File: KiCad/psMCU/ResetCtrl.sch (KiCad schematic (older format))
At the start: 14 parts

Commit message: Pulled in from clock test, root layout first draft
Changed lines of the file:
@@
 $Descr A4 11693 8268
 encoding utf-8
-Sheet 111 193
+Sheet 113 209
 Title "psMCU"
 Date ""
@@
 AR Path="/5F1CE57C/5FD43FAC" Ref="#PWR?"  Part="1"
 AR Path="/608BF85D/5FD43FAC" Ref="#PWR?"  Part="1"
-AR Path="/5FD3CD07/5FD43FAC" Ref="#PWR?"  Part="1"
-F 0 "#PWR?" H 8850 3100 50  0001 C CNN
+AR Path="/5FD3CD07/5FD43FAC" Ref="#PWR01660"  Part="1"
+F 0 "#PWR01660" H 8850 3100 50  0001 C CNN
 F 1 "GND" V 8855 3222 50  0000 R CNN
 F 2 "" H 8850 3350 50  0001 C CNN
@@
 AR Path="/5F1CE57C/5FD43FB4" Ref="#PWR?"  Part="1"
 AR Path="/608BF85D/5FD43FB4" Ref="#PWR?"  Part="1"
-AR Path="/5FD3CD07/5FD43FB4" Ref="#PWR?"  Part="1"
-F 0 "#PWR?" H 8550 3500 50  0001 C CNN
+AR Path="/5FD3CD07/5FD43FB4" Ref="#PWR01661"  Part="1"
+F 0 "#PWR01661" H 8550 3500 50  0001 C CNN
 F 1 "GND" H 8555 3577 50  0000 C CNN
 F 2 "" H 8550 3750 50  0001 C CNN
@@
 AR Path="/5F1CE57C/5FD43FC2" Ref="#PWR?"  Part="1"
 AR Path="/608BF85D/5FD43FC2" Ref="#PWR?"  Part="1"
-AR Path="/5FD3CD07/5FD43FC2" Ref="#PWR?"  Part="1"
-F 0 "#PWR?" H 8550 3150 50  0001 C CNN
+AR Path="/5FD3CD07/5FD43FC2" Ref="#PWR01662"  Part="1"
+F 0 "#PWR01662" H 8550 3150 50  0001 C CNN
 F 1 "+5V" H 8450 3400 50  0000 C CNN
 F 2 "" H 8550 3300 50  0001 C CNN
@@
 	8800 3550 9350 3550
 Wire Wire Line
-	9350 4000 7800 4000
+	9350 4000 8250 4000
 Wire Wire Line
 	7800 4000 7800 3550
@@
 AR Path="/5F1CE57C/5FF7364D" Ref="#PWR?"  Part="1"
 AR Path="/5F396002/5FF7364D" Ref="#PWR?"  Part="1"
-AR Path="/5FD3CD07/5FF7364D" Ref="#PWR?"  Part="1"
-F 0 "#PWR?" H 5850 3150 50  0001 C CNN
+AR Path="/5FD3CD07/5FF7364D" Ref="#PWR01663"  Part="1"
+F 0 "#PWR01663" H 5850 3150 50  0001 C CNN
 F 1 "GND" H 5855 3227 50  0000 C CNN
 F 2 "" H 5850 3400 50  0001 C CNN
@@
 AR Path="/5F1CE57C/5FF73655" Ref="#PWR?"  Part="1"
 AR Path="/5F396002/5FF73655" Ref="#PWR?"  Part="1"
-AR Path="/5FD3CD07/5FF73655" Ref="#PWR?"  Part="1"
-F 0 "#PWR?" H 5850 2800 50  0001 C CNN
+AR Path="/5FD3CD07/5FF73655" Ref="#PWR01664"  Part="1"
+F 0 "#PWR01664" H 5850 2800 50  0001 C CNN
 F 1 "+5V" H 5865 3123 50  0000 C CNN
 F 2 "" H 5850 2950 50  0001 C CNN
@@
 AR Path="/5F1CE57C/5FF73664" Ref="#PWR?"  Part="1"
 AR Path="/5F396002/5FF73664" Ref="#PWR?"  Part="1"
-AR Path="/5FD3CD07/5FF73664" Ref="#PWR?"  Part="1"
-F 0 "#PWR?" H 6150 2750 50  0001 C CNN
+AR Path="/5FD3CD07/5FF73664" Ref="#PWR01665"  Part="1"
+F 0 "#PWR01665" H 6150 2750 50  0001 C CNN
 F 1 "GND" V 6155 2872 50  0000 R CNN
 F 2 "" H 6150 3000 50  0001 C CNN
@@
 AR Path="/5F1CE57C/5FFDD1F3" Ref="#PWR?"  Part="1"
 AR Path="/5F396002/5FFDD1F3" Ref="#PWR?"  Part="1"
-AR Path="/5FD3CD07/5FFDD1F3" Ref="#PWR?"  Part="1"
-F 0 "#PWR?" H 3450 2700 50  0001 C CNN
+AR Path="/5FD3CD07/5FFDD1F3" Ref="#PWR01666"  Part="1"
+F 0 "#PWR01666" H 3450 2700 50  0001 C CNN
 F 1 "GND" V 3455 2822 50  0000 R CNN
 F 2 "" H 3450 2950 50  0001 C CNN
@@
 AR Path="/5F1CE57C/5FFDD202" Ref="#PWR?"  Part="1"
 AR Path="/5F396002/5FFDD202" Ref="#PWR?"  Part="1"
-AR Path="/5FD3CD07/5FFDD202" Ref="#PWR?"  Part="1"
-F 0 "#PWR?" H 3150 2750 50  0001 C CNN
+AR Path="/5FD3CD07/5FFDD202" Ref="#PWR01667"  Part="1"
+F 0 "#PWR01667" H 3150 2750 50  0001 C CNN
 F 1 "+5V" H 3165 3073 50  0000 C CNN
 F 2 "" H 3150 2900 50  0001 C CNN
@@
 AR Path="/5F1CE57C/5FFDD209" Ref="#PWR?"  Part="1"
 AR Path="/5F396002/5FFDD209" Ref="#PWR?"  Part="1"
-AR Path="/5FD3CD07/5FFDD209" Ref="#PWR?"  Part="1"
-F 0 "#PWR?" H 3150 3050 50  0001 C CNN
+AR Path="/5FD3CD07/5FFDD209" Ref="#PWR01668"  Part="1"
+F 0 "#PWR01668" H 3150 3050 50  0001 C CNN
 F 1 "GND" H 3250 3150 50  0000 R CNN
 F 2 "" H 3150 3300 50  0001 C CNN
@@
 AR Path="/5F1CE57C/5FFDEBBC" Ref="#PWR?"  Part="1"
 AR Path="/5F396002/5FFDEBBC" Ref="#PWR?"  Part="1"
-AR Path="/5FD3CD07/5FFDEBBC" Ref="#PWR?"  Part="1"
-F 0 "#PWR?" H 2400 3250 50  0001 C CNN
+AR Path="/5FD3CD07/5FFDEBBC" Ref="#PWR01669"  Part="1"
+F 0 "#PWR01669" H 2400 3250 50  0001 C CNN
 F 1 "GND" H 2500 3350 50  0000 R CNN
 F 2 "" H 2400 3500 50  0001 C CNN
@@
 AR Path="/5F1CE57C/5FFE9777" Ref="#PWR?"  Part="1"
 AR Path="/5F396002/5FFE9777" Ref="#PWR?"  Part="1"
-AR Path="/5FD3CD07/5FFE9777" Ref="#PWR?"  Part="1"
-F 0 "#PWR?" H 2400 2350 50  0001 C CNN
+AR Path="/5FD3CD07/5FFE9777" Ref="#PWR01670"  Part="1"
+F 0 "#PWR01670" H 2400 2350 50  0001 C CNN
 F 1 "+5V" H 2415 2673 50  0000 C CNN
 F 2 "" H 2400 2500 50  0001 C CNN
@@
 AR Path="/5F1CE57C/6000A97B" Ref="#PWR?"  Part="1"
 AR Path="/608BF85D/6000A97B" Ref="#PWR?"  Part="1"
-AR Path="/5FD3CD07/6000A97B" Ref="#PWR?"  Part="1"
-F 0 "#PWR?" H 4300 2700 50  0001 C CNN
+AR Path="/5FD3CD07/6000A97B" Ref="#PWR01671"  Part="1"
+F 0 "#PWR01671" H 4300 2700 50  0001 C CNN
 F 1 "GND" V 4305 2822 50  0000 R CNN
 F 2 "" H 4300 2950 50  0001 C CNN
@@
 AR Path="/5F1CE57C/6000A983" Ref="#PWR?"  Part="1"
 AR Path="/608BF85D/6000A983" Ref="#PWR?"  Part="1"
-AR Path="/5FD3CD07/6000A983" Ref="#PWR?"  Part="1"
-F 0 "#PWR?" H 4000 3100 50  0001 C CNN
+AR Path="/5FD3CD07/6000A983" Ref="#PWR01672"  Part="1"
+F 0 "#PWR01672" H 4000 3100 50  0001 C CNN
 F 1 "GND" H 4005 3177 50  0000 C CNN
 F 2 "" H 4000 3350 50  0001 C CNN
@@
 AR Path="/5F1CE57C/6000A991" Ref="#PWR?"  Part="1"
 AR Path="/608BF85D/6000A991" Ref="#PWR?"  Part="1"
-AR Path="/5FD3CD07/6000A991" Ref="#PWR?"  Part="1"
-F 0 "#PWR?" H 4000 2750 50  0001 C CNN
+AR Path="/5FD3CD07/6000A991" Ref="#PWR01673"  Part="1"
+F 0 "#PWR01673" H 4000 2750 50  0001 C CNN
 F 1 "+5V" H 3900 3000 50  0000 C CNN
 F 2 "" H 4000 2900 50  0001 C CNN
@@
 AR Path="/5F1CE57C/61C134A2" Ref="#PWR?"  Part="1"
 AR Path="/5F396002/61C134A2" Ref="#PWR?"  Part="1"
-AR Path="/5FD3CD07/61C134A2" Ref="#PWR?"  Part="1"
-F 0 "#PWR?" H 7100 3200 50  0001 C CNN
+AR Path="/5FD3CD07/61C134A2" Ref="#PWR01674"  Part="1"
+F 0 "#PWR01674" H 7100 3200 50  0001 C CNN
 F 1 "GND" H 7105 3277 50  0000 C CNN
 F 2 "" H 7100 3450 50  0001 C CNN
@@
 AR Path="/5F1CE57C/61C134AA" Ref="#PWR?"  Part="1"
 AR Path="/5F396002/61C134AA" Ref="#PWR?"  Part="1"
-AR Path="/5FD3CD07/61C134AA" Ref="#PWR?"  Part="1"
-F 0 "#PWR?" H 7100 2850 50  0001 C CNN
+AR Path="/5FD3CD07/61C134AA" Ref="#PWR01675"  Part="1"
+F 0 "#PWR01675" H 7100 2850 50  0001 C CNN
 F 1 "+5V" H 7115 3173 50  0000 C CNN
 F 2 "" H 7100 3000 50  0001 C CNN
@@
 AR Path="/5F1CE57C/61C134B9" Ref="#PWR?"  Part="1"
 AR Path="/5F396002/61C134B9" Ref="#PWR?"  Part="1"
-AR Path="/5FD3CD07/61C134B9" Ref="#PWR?"  Part="1"
-F 0 "#PWR?" H 7400 2800 50  0001 C CNN
+AR Path="/5FD3CD07/61C134B9" Ref="#PWR01676"  Part="1"
+F 0 "#PWR01676" H 7400 2800 50  0001 C CNN
 F 1 "GND" V 7405 2922 50  0000 R CNN
 F 2 "" H 7400 3050 50  0001 C CNN
@@
 Wire Wire Line
 	5300 3150 5550 3150
+$Sheet
+S 8650 4350 700  200
+U 602A39E5
+F0 "LED: Reset" 50
+F1 "1BitLED.sch" 50
+F2 "VAL" I L 8650 4450 50
+$EndSheet
+Wire Wire Line
+	8650 4450 8250 4450
+Wire Wire Line
+	8250 4450 8250 4000
+Connection ~ 8250 4000
+Wire Wire Line
+	8250 4000 7800 4000
 $EndSCHEMATC

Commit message: Added some footprints, small optimisations
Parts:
- U? (x3): footprint (none) -> Package_TO_SOT_SMD:SOT-353_SC-70-5
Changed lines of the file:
@@
 $Descr A4 11693 8268
 encoding utf-8
-Sheet 113 202
+Sheet 147 202
 Title "psMCU"
 Date ""
@@
 F 0 "U?" H 6000 3100 50  0000 C CNN
 F 1 "74LVC1G32" H 6150 3000 50  0000 C CNN
-F 2 "" H 5850 3200 50  0001 C CNN
+F 2 "Package_TO_SOT_SMD:SOT-353_SC-70-5" H 5850 3200 50  0001 C CNN
 F 3 "http://www.ti.com/lit/sg/scyt129e/scyt129e.pdf" H 5850 3200 50  0001 C CNN
 	1    5850 3200
@@
 F 0 "U?" H 3300 3100 50  0000 C CNN
 F 1 "74LVC1G17" H 3450 3000 50  0000 C CNN
-F 2 "" H 3150 3150 50  0001 C CNN
+F 2 "Package_TO_SOT_SMD:SOT-353_SC-70-5" H 3150 3150 50  0001 C CNN
 F 3 "http://www.ti.com/lit/sg/scyt129e/scyt129e.pdf" H 3150 3150 50  0001 C CNN
 	1    3150 3150
@@
 F 0 "U?" H 7250 3150 50  0000 C CNN
 F 1 "74LVC1G32" H 7400 3050 50  0000 C CNN
-F 2 "" H 7100 3250 50  0001 C CNN
+F 2 "Package_TO_SOT_SMD:SOT-353_SC-70-5" H 7100 3250 50  0001 C CNN
 F 3 "http://www.ti.com/lit/sg/scyt129e/scyt129e.pdf" H 7100 3250 50  0001 C CNN
 	1    7100 3250

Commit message: Started some documentation work.
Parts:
- R?: value 56k -> 1M
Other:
- note added: "Automatic Reset on Power-on"
- note added: "Combine Reset Sources"
- note removed: "Automatic Reset-on-Power"
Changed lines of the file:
@@
 Comment1 ""
 Comment2 ""
-Comment3 ""
-Comment4 ""
+Comment3 "generate the RESET and ~RESET~ signals used globally."
+Comment4 "Generates reset during power-on and combines the different reset sources to"
 $EndDescr
 Text Label 9250 3550 2    50   ~ 0
@@
 P 2400 2950
 F 0 "R?" H 2459 2996 50  0000 L CNN
-F 1 "56k" H 2459 2905 50  0000 L CNN
+F 1 "1M" H 2459 2905 50  0000 L CNN
 F 2 "Resistor_SMD:R_0603_1608Metric" H 2400 2950 50  0001 C CNN
 F 3 "~" H 2400 2950 50  0001 C CNN
@@
 Wire Wire Line
 	7800 3250 7800 3550
-Text Notes 3000 2450 0    50   ~ 0
-Automatic Reset-on-Power
-Text HLabel 7000 2450 2    50   Output ~ 0
+Text Notes 1950 1850 0    100  ~ 0
+Automatic Reset on Power-on
+Text HLabel 5400 2450 2    50   Output ~ 0
 POWER_ON_RESET
 Wire Wire Line
 	5300 2450 5300 3150
 Wire Wire Line
-	5300 2450 7000 2450
+	5300 2450 5400 2450
 Connection ~ 5300 3150
 Wire Wire Line
@@
 Wire Wire Line
 	8250 4000 7800 4000
+Text Notes 5750 1850 0    100  ~ 0
+Combine Reset Sources
 $EndSCHEMATC

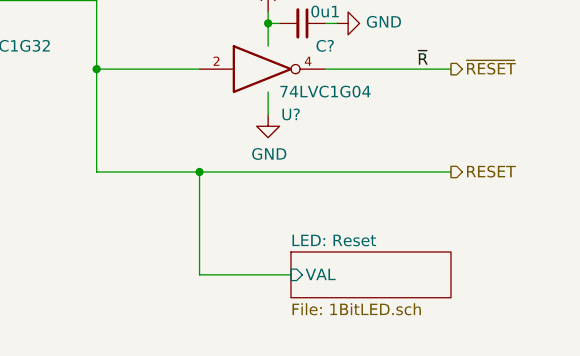
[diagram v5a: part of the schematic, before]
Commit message: Removed Single LED sheets
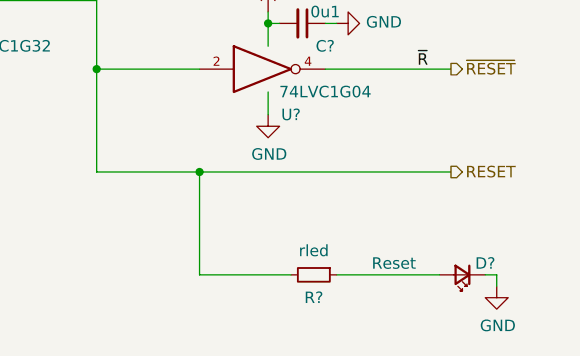
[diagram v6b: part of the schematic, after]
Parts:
- added D?: Reset, Diode_SMD:D_0603_1608Metric, symbol Device:LED_Small
- added R?: rled, Resistor_SMD:R_0603_1608Metric, symbol Device:R_Small
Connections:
- net GND: now also D?.1 (K)
- net RESET: now also R?.2
- new net: D?.2 (A), R?.1

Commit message: First Schematic Draft done.
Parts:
- removed C? (x2): 0u1, Capacitor_SMD:C_0603_1608Metric, symbol Device:C_Small
- removed U? (x2): 74LVC1G32, Package_TO_SOT_SMD:SOT-353_SC-70-5, symbol 74xGxx:74LVC1G32
- added C285: 0u1, NoRef_Footprints:C_0603_1608Metric_NoRef, symbol Device:C_Small
- added U279: 74LVC1G332, symbol 74xGxx:74LVC1G332
- C282, C283, C284, C286: renamed from C?; footprint Capacitor_SMD:C_0603_1608Metric -> NoRef_Footprints:C_0603_1608Metric_NoRef
- D362: renamed from D?; footprint Diode_SMD:D_0603_1608Metric -> NoRef_Footprints:D_0603_1608Metric_NoRef
- R367: renamed from R?; footprint Resistor_SMD:R_0603_1608Metric -> NoRef_Footprints:R_0603_1608Metric
- gave numbers to parts that had none: 6
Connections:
- net +5V: now also C285.2, U279.5 (VCC)
- net GND: now also C285.1, U279.2 (GND)
- net POWER_ON_RESET: now also U279.6
- net PROG_DO_RESET: now also U279.3
- net RESET: now also U279.4
- net UI_DO_RESET: now also U279.1
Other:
- note added: "Generate different Reset signals"
- note removed: "Combine Reset Sources"
- moved on the sheet: C286, D362, R367, U280

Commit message: Small improvements.
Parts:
- renumbered C282 to C280, C283 to C281, C284 to C282, C285 to C283, C286 to C284, U277 to U275, U278 to U276, U279 to U277, U280 to U278
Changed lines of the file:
@@
 AR Path="/5F1CE57C/5FD43FAC" Ref="#PWR?"  Part="1"
 AR Path="/608BF85D/5FD43FAC" Ref="#PWR?"  Part="1"
-AR Path="/5FD3CD07/5FD43FAC" Ref="#PWR01237"  Part="1"
-F 0 "#PWR01237" H 7750 3100 50  0001 C CNN
+AR Path="/5FD3CD07/5FD43FAC" Ref="#PWR01222"  Part="1"
+F 0 "#PWR01222" H 7750 3100 50  0001 C CNN
 F 1 "GND" V 7755 3222 50  0000 R CNN
 F 2 "" H 7750 3350 50  0001 C CNN
@@
 AR Path="/5F1CE57C/5FD43FB4" Ref="#PWR?"  Part="1"
 AR Path="/608BF85D/5FD43FB4" Ref="#PWR?"  Part="1"
-AR Path="/5FD3CD07/5FD43FB4" Ref="#PWR01236"  Part="1"
-F 0 "#PWR01236" H 7450 3500 50  0001 C CNN
+AR Path="/5FD3CD07/5FD43FB4" Ref="#PWR01221"  Part="1"
+F 0 "#PWR01221" H 7450 3500 50  0001 C CNN
 F 1 "GND" H 7455 3577 50  0000 C CNN
 F 2 "" H 7450 3750 50  0001 C CNN
@@
 AR Path="/5F1CE57C/5FD43FBC" Ref="C?"  Part="1"
 AR Path="/608BF85D/5FD43FBC" Ref="C?"  Part="1"
-AR Path="/5FD3CD07/5FD43FBC" Ref="C286"  Part="1"
-F 0 "C286" V 7700 3450 50  0000 C CNN
+AR Path="/5FD3CD07/5FD43FBC" Ref="C284"  Part="1"
+F 0 "C284" V 7700 3450 50  0000 C CNN
 F 1 "0u1" V 7550 3450 50  0000 C CNN
 F 2 "NoRef_Footprints:C_0603_1608Metric_NoRef" H 7600 3350 50  0001 C CNN
@@
 AR Path="/5F1CE57C/5FD43FC2" Ref="#PWR?"  Part="1"
 AR Path="/608BF85D/5FD43FC2" Ref="#PWR?"  Part="1"
-AR Path="/5FD3CD07/5FD43FC2" Ref="#PWR01235"  Part="1"
-F 0 "#PWR01235" H 7450 3150 50  0001 C CNN
+AR Path="/5FD3CD07/5FD43FC2" Ref="#PWR01220"  Part="1"
+F 0 "#PWR01220" H 7450 3150 50  0001 C CNN
 F 1 "+5V" H 7350 3400 50  0000 C CNN
 F 2 "" H 7450 3300 50  0001 C CNN
@@
 AR Path="/5F1CE57C/5FD43FCA" Ref="U?"  Part="1"
 AR Path="/608BF85D/5FD43FCA" Ref="U?"  Part="1"
-AR Path="/5FD3CD07/5FD43FCA" Ref="U280"  Part="1"
-F 0 "U280" H 7550 3350 50  0000 C CNN
+AR Path="/5FD3CD07/5FD43FCA" Ref="U278"  Part="1"
+F 0 "U278" H 7550 3350 50  0000 C CNN
 F 1 "74LVC1G04" H 7700 3450 50  0000 C CNN
 F 2 "Package_TO_SOT_SMD:SOT-353_SC-70-5" H 7450 3550 50  0001 C CNN
@@
 UI_DO_RESET
 $Comp
-L 74xGxx:74LVC1G17 U277
+L 74xGxx:74LVC1G17 U275
 U 1 1 5FFDD1EC
 P 3150 3150
-F 0 "U277" H 3300 3100 50  0000 C CNN
+F 0 "U275" H 3300 3100 50  0000 C CNN
 F 1 "74LVC1G17" H 3450 3000 50  0000 C CNN
 F 2 "Package_TO_SOT_SMD:SOT-353_SC-70-5" H 3150 3150 50  0001 C CNN
@@
 AR Path="/5F1CE57C/5FFDD1F3" Ref="#PWR?"  Part="1"
 AR Path="/5F396002/5FFDD1F3" Ref="#PWR?"  Part="1"
-AR Path="/5FD3CD07/5FFDD1F3" Ref="#PWR01228"  Part="1"
-F 0 "#PWR01228" H 3450 2700 50  0001 C CNN
+AR Path="/5FD3CD07/5FFDD1F3" Ref="#PWR01213"  Part="1"
+F 0 "#PWR01213" H 3450 2700 50  0001 C CNN
 F 1 "GND" V 3455 2822 50  0000 R CNN
 F 2 "" H 3450 2950 50  0001 C CNN
@@
 AR Path="/5F1CE57C/5FFDD1FC" Ref="C?"  Part="1"
 AR Path="/5F396002/5FFDD1FC" Ref="C?"  Part="1"
-AR Path="/5FD3CD07/5FFDD1FC" Ref="C283"  Part="1"
-F 0 "C283" V 3400 3050 50  0000 C CNN
+AR Path="/5FD3CD07/5FFDD1FC" Ref="C281"  Part="1"
+F 0 "C281" V 3400 3050 50  0000 C CNN
 F 1 "0u1" V 3250 3050 50  0000 C CNN
 F 2 "NoRef_Footprints:C_0603_1608Metric_NoRef" H 3300 2950 50  0001 C CNN
@@
 AR Path="/5F1CE57C/5FFDD202" Ref="#PWR?"  Part="1"
 AR Path="/5F396002/5FFDD202" Ref="#PWR?"  Part="1"
-AR Path="/5FD3CD07/5FFDD202" Ref="#PWR01226"  Part="1"
-F 0 "#PWR01226" H 3150 2750 50  0001 C CNN
+AR Path="/5FD3CD07/5FFDD202" Ref="#PWR01211"  Part="1"
+F 0 "#PWR01211" H 3150 2750 50  0001 C CNN
 F 1 "+5V" H 3165 3073 50  0000 C CNN
 F 2 "" H 3150 2900 50  0001 C CNN
@@
 AR Path="/5F1CE57C/5FFDD209" Ref="#PWR?"  Part="1"
 AR Path="/5F396002/5FFDD209" Ref="#PWR?"  Part="1"
-AR Path="/5FD3CD07/5FFDD209" Ref="#PWR01227"  Part="1"
-F 0 "#PWR01227" H 3150 3050 50  0001 C CNN
+AR Path="/5FD3CD07/5FFDD209" Ref="#PWR01212"  Part="1"
+F 0 "#PWR01212" H 3150 3050 50  0001 C CNN
 F 1 "GND" H 3250 3150 50  0000 R CNN
 F 2 "" H 3150 3300 50  0001 C CNN
@@
 	3150 3300 3150 3250
 $Comp
-L Device:C_Small C282
+L Device:C_Small C280
 U 1 1 5FFDD9FC
 P 2400 3350
-F 0 "C282" H 2492 3396 50  0000 L CNN
+F 0 "C280" H 2492 3396 50  0000 L CNN
 F 1 "0u1" H 2492 3305 50  0000 L CNN
 F 2 "NoRef_Footprints:C_0603_1608Metric_NoRef" H 2400 3350 50  0001 C CNN
@@
 AR Path="/5F1CE57C/5FFDEBBC" Ref="#PWR?"  Part="1"
 AR Path="/5F396002/5FFDEBBC" Ref="#PWR?"  Part="1"
-AR Path="/5FD3CD07/5FFDEBBC" Ref="#PWR01225"  Part="1"
-F 0 "#PWR01225" H 2400 3250 50  0001 C CNN
+AR Path="/5FD3CD07/5FFDEBBC" Ref="#PWR01210"  Part="1"
+F 0 "#PWR01210" H 2400 3250 50  0001 C CNN
 F 1 "GND" H 2500 3350 50  0000 R CNN
 F 2 "" H 2400 3500 50  0001 C CNN
@@
 AR Path="/5F1CE57C/5FFE9777" Ref="#PWR?"  Part="1"
 AR Path="/5F396002/5FFE9777" Ref="#PWR?"  Part="1"
-AR Path="/5FD3CD07/5FFE9777" Ref="#PWR01224"  Part="1"
-F 0 "#PWR01224" H 2400 2350 50  0001 C CNN
+AR Path="/5FD3CD07/5FFE9777" Ref="#PWR01209"  Part="1"
+F 0 "#PWR01209" H 2400 2350 50  0001 C CNN
 F 1 "+5V" H 2415 2673 50  0000 C CNN
 F 2 "" H 2400 2500 50  0001 C CNN
@@
 AR Path="/5F1CE57C/6000A97B" Ref="#PWR?"  Part="1"
 AR Path="/608BF85D/6000A97B" Ref="#PWR?"  Part="1"
-AR Path="/5FD3CD07/6000A97B" Ref="#PWR01231"  Part="1"
-F 0 "#PWR01231" H 4300 2700 50  0001 C CNN
+AR Path="/5FD3CD07/6000A97B" Ref="#PWR01216"  Part="1"
+F 0 "#PWR01216" H 4300 2700 50  0001 C CNN
 F 1 "GND" V 4305 2822 50  0000 R CNN
 F 2 "" H 4300 2950 50  0001 C CNN
@@
 AR Path="/5F1CE57C/6000A983" Ref="#PWR?"  Part="1"
 AR Path="/608BF85D/6000A983" Ref="#PWR?"  Part="1"
-AR Path="/5FD3CD07/6000A983" Ref="#PWR01230"  Part="1"
-F 0 "#PWR01230" H 4000 3100 50  0001 C CNN
+AR Path="/5FD3CD07/6000A983" Ref="#PWR01215"  Part="1"
+F 0 "#PWR01215" H 4000 3100 50  0001 C CNN
 F 1 "GND" H 4005 3177 50  0000 C CNN
 F 2 "" H 4000 3350 50  0001 C CNN
@@
 AR Path="/5F1CE57C/6000A98B" Ref="C?"  Part="1"
 AR Path="/608BF85D/6000A98B" Ref="C?"  Part="1"
-AR Path="/5FD3CD07/6000A98B" Ref="C284"  Part="1"
-F 0 "C284" V 4250 3050 50  0000 C CNN
+AR Path="/5FD3CD07/6000A98B" Ref="C282"  Part="1"
+F 0 "C282" V 4250 3050 50  0000 C CNN
 F 1 "0u1" V 4100 3050 50  0000 C CNN
 F 2 "NoRef_Footprints:C_0603_1608Metric_NoRef" H 4150 2950 50  0001 C CNN
@@
 AR Path="/5F1CE57C/6000A991" Ref="#PWR?"  Part="1"
 AR Path="/608BF85D/6000A991" Ref="#PWR?"  Part="1"
-AR Path="/5FD3CD07/6000A991" Ref="#PWR01229"  Part="1"
-F 0 "#PWR01229" H 4000 2750 50  0001 C CNN
+AR Path="/5FD3CD07/6000A991" Ref="#PWR01214"  Part="1"
+F 0 "#PWR01214" H 4000 2750 50  0001 C CNN
 F 1 "+5V" H 3900 3000 50  0000 C CNN
 F 2 "" H 4000 2900 50  0001 C CNN
@@
 AR Path="/5F1CE57C/6000A999" Ref="U?"  Part="1"
 AR Path="/608BF85D/6000A999" Ref="U?"  Part="1"
-AR Path="/5FD3CD07/6000A999" Ref="U278"  Part="1"
-F 0 "U278" H 4100 2950 50  0000 C CNN
+AR Path="/5FD3CD07/6000A999" Ref="U276"  Part="1"
+F 0 "U276" H 4100 2950 50  0000 C CNN
 F 1 "74LVC1G04" H 4250 3050 50  0000 C CNN
 F 2 "Package_TO_SOT_SMD:SOT-353_SC-70-5" H 4000 3150 50  0001 C CNN
@@
 AR Path="/5F1CE57C/61C134B9" Ref="#PWR?"  Part="1"
 AR Path="/5F396002/61C134B9" Ref="#PWR?"  Part="1"
-AR Path="/5FD3CD07/61C134B9" Ref="#PWR01233"  Part="1"
-F 0 "#PWR01233" H 5850 3175 50  0001 C CNN
+AR Path="/5FD3CD07/61C134B9" Ref="#PWR01218"  Part="1"
+F 0 "#PWR01218" H 5850 3175 50  0001 C CNN
 F 1 "GND" V 5855 3297 50  0000 R CNN
 F 2 "" H 5850 3425 50  0001 C CNN
@@
 AR Path="/5F18F3CA/62BB5F2D" Ref="#PWR?"  Part="1"
 AR Path="/60E33DBC/5FD12DEC/62BB5F2D" Ref="#PWR?"  Part="1"
-AR Path="/5FD3CD07/62BB5F2D" Ref="#PWR01238"  Part="1"
-F 0 "#PWR01238" H 8450 4250 50  0001 C CNN
+AR Path="/5FD3CD07/62BB5F2D" Ref="#PWR01223"  Part="1"
+F 0 "#PWR01223" H 8450 4250 50  0001 C CNN
 F 1 "GND" H 8455 4327 50  0000 C CNN
 F 2 "" H 8450 4500 50  0001 C CNN
@@
 	8450 4450 8400 4450
 $Comp
-L 74xGxx:74LVC1G332 U279
+L 74xGxx:74LVC1G332 U277
 U 1 1 61870EF6
 P 5850 3250
-F 0 "U279" H 6100 3050 50  0000 C CNN
+F 0 "U277" H 6100 3050 50  0000 C CNN
 F 1 "74LVC1G332" H 6250 3150 50  0000 C CNN
 F 2 "" H 5850 3250 50  0001 C CNN
@@
 AR Path="/5F1CE57C/618734BC" Ref="#PWR?"  Part="1"
 AR Path="/5F396002/618734BC" Ref="#PWR?"  Part="1"
-AR Path="/5FD3CD07/618734BC" Ref="#PWR01232"  Part="1"
-F 0 "#PWR01232" H 5850 2825 50  0001 C CNN
+AR Path="/5FD3CD07/618734BC" Ref="#PWR01217"  Part="1"
+F 0 "#PWR01217" H 5850 2825 50  0001 C CNN
 F 1 "+5V" H 5865 3148 50  0000 C CNN
 F 2 "" H 5850 2975 50  0001 C CNN
@@
 AR Path="/5F1CE57C/618734C2" Ref="C?"  Part="1"
 AR Path="/5F396002/618734C2" Ref="C?"  Part="1"
-AR Path="/5FD3CD07/618734C2" Ref="C285"  Part="1"
-F 0 "C285" V 6100 3125 50  0000 C CNN
+AR Path="/5FD3CD07/618734C2" Ref="C283"  Part="1"
+F 0 "C283" V 6100 3125 50  0000 C CNN
 F 1 "0u1" V 5950 3125 50  0000 C CNN
 F 2 "NoRef_Footprints:C_0603_1608Metric_NoRef" H 6000 3025 50  0001 C CNN
@@
 AR Path="/5F1CE57C/618734CB" Ref="#PWR?"  Part="1"
 AR Path="/5F396002/618734CB" Ref="#PWR?"  Part="1"
-AR Path="/5FD3CD07/618734CB" Ref="#PWR01234"  Part="1"
-F 0 "#PWR01234" H 6150 2775 50  0001 C CNN
+AR Path="/5FD3CD07/618734CB" Ref="#PWR01219"  Part="1"
+F 0 "#PWR01219" H 6150 2775 50  0001 C CNN
 F 1 "GND" V 6155 2897 50  0000 R CNN
 F 2 "" H 6150 3025 50  0001 C CNN
